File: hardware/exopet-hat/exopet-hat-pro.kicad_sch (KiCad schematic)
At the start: 88 parts, among them J1 12V DC in, J10 CH3 12V OUT, J11 CH4 dry contact, J13 FLOAT1 switch, J14 FLOAT2 switch, J15 pH probe BNC, J3 RPi GPIO (HAT), J4 TEMP (3V3/DATA/GND), J8 CH1 12V OUT, J9 CH2 12V OUT, K1 G5LE-1-CF DC12, K2 G5LE-1-CF DC12, K3 G5LE-1-CF DC12, K4 G5LE-1-CF DC12, Q1 AOD403, U10 MCP6002 (pH buffers), U2 TBD62003AFG, U4 CAT24C32, U5 5V ESD clamp (SOD-323), U6 TPS54302DDC, U7 ADS1115 (floats, 0x48), U8 ADS1115 (pH, 0x49), U9 ISO1540 I2C isolator

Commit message: HAT pro: resolve isolated-rail overvoltage — AMS1117-3.3 LDO on the pH island
Fixes the inline-review finding: the <2mA (<1% load) island let an
unregulated 1W module float past the ADS1115/ISO1540 5.5V max and
inject ripple into the pH ADC. Added U11 AMS1117-3.3 (raw +5V_ISO ->
clean +3V3_ISO); moved U8/U9-VCC2/U10, R26/R27 pull-ups and the R24
bias-top onto +3V3_ISO; C22 = LDO input bulk, C28 = output cap. pH
bias now 1.65V ±0.414V, within ADS1115 FSR and MCP6002 common-mode.
AMS1117's ~15V Vin absorbs the module's no-load rise; ~5mA Iq
preloads it. Netlist confirms the rail split (+5V_ISO = 3 pins only).
ERC benign-only; polarity + golden tables updated. Pin numbers taken
from the KiCad symbol, not assumed (GND1/VO2/VI3). Board layout next.

Co-Authored-By: Claude Fable 5 <noreply@anthropic.com>
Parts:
- added C28: 22uF 10V (LDO out), Capacitor_SMD:C_1210_3225Metric, symbol Device:C
- added U11: AMS1117-3.3 (iso rail), Package_TO_SOT_SMD:SOT-223-3_TabPin2, symbol Regulator_Linear:AMS1117-3.3
- C22: value 10uF 10V -> 10uF 25V (LDO in bulk)
- PS1: value B0505S-1WR2 iso DC-DC (SIP-4) -> 1W iso DC-DC 5Vout SIP-4 (reg or unreg OK; LDO follows)
- R24: value 100k (bias hi) -> 100k (bias hi -> 1.65V mid)
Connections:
- net +5V_ISO: now also U11.3 (VI); no longer C21.1, C25.1, R24.1, R26.1, R27.1, U10.8 (V+), U8.1 (ADDR), U8.8 (VDD), U9.8 (VCC2)
- net ISO_GND: now also C28.2, U11.1 (GND)
- new net +3V3_ISO: C21.1, C25.1, C28.1, R24.1, R26.1, R27.1, U10.8 (V+), U11.2 (VO), U8.1 (ADDR), U8.8 (VDD), U9.8 (VCC2)

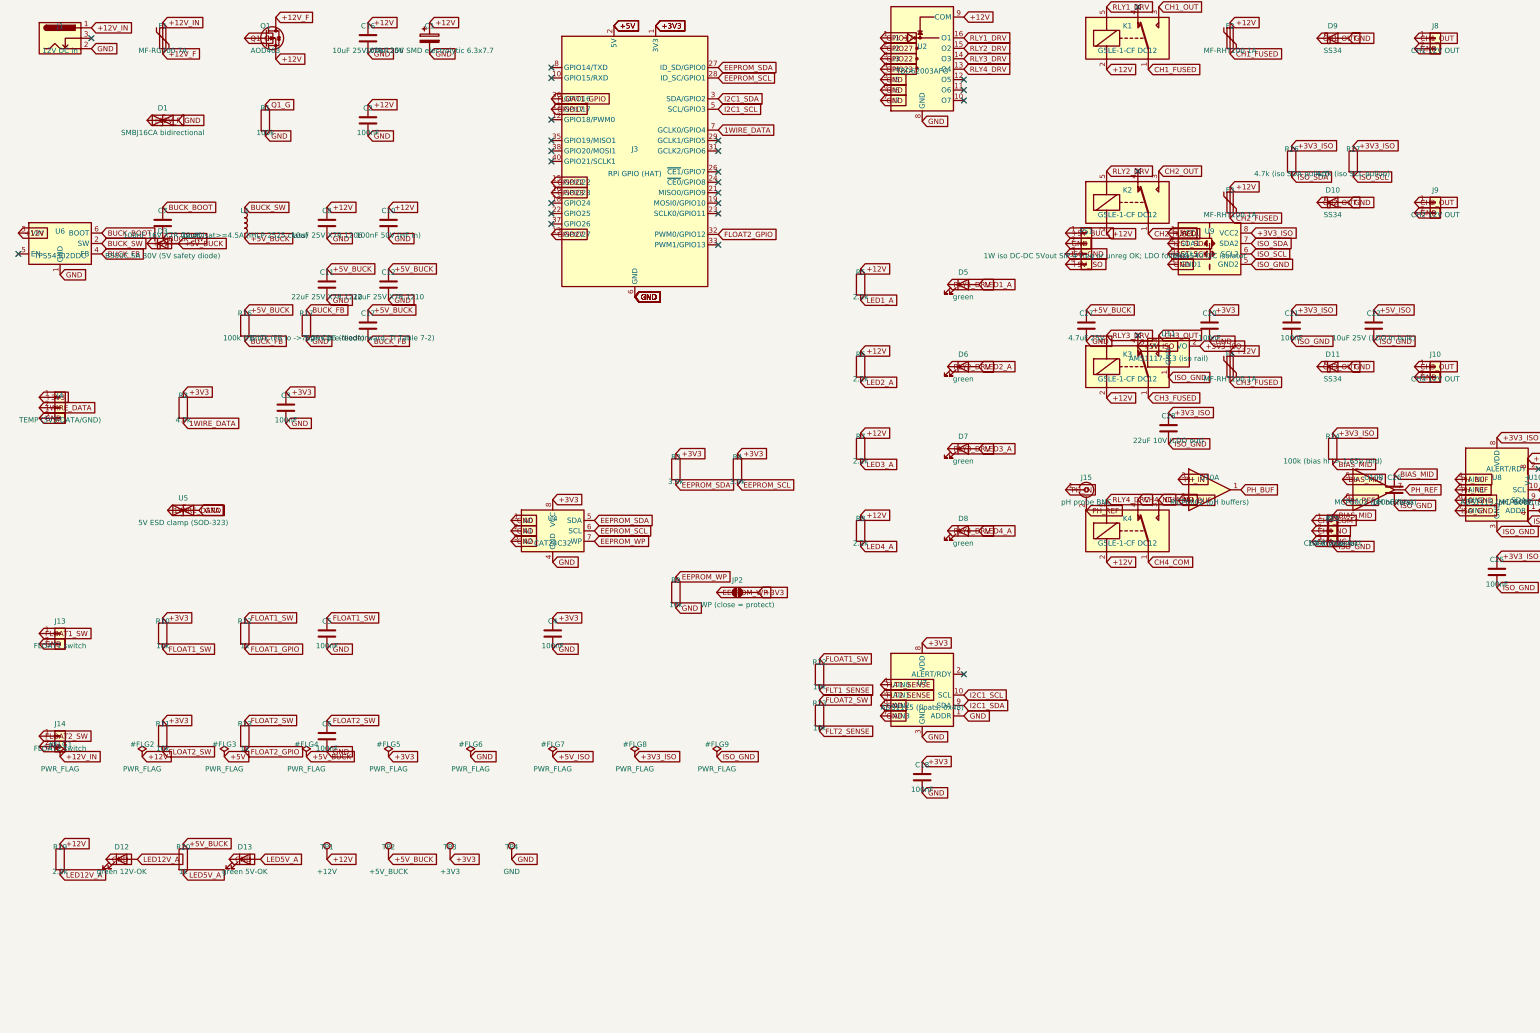
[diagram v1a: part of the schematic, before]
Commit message: HAT pro: expand to 6 relays + 2 more supervised sensor inputs (schematic)
Pro gains CH5 (switched 12V, GPIO24) + CH6 (dry contact, GPIO25) on the
existing TBD62003 driver (now 6/7 channels), each with the standard
fuse/flyback/terminal/LED per their type; and SW3/SW4 general
supervised switch inputs on the sensor ADC's spare A2/A3 channels
(ADC-only, 3-state EOL detection like the floats). J3 pins 18/22 carry
the new GPIO. All 6-relay/sensor parts are add_pro-gated so std stays a
4-relay 65x56 HAT-compliant board. add_pro hoisted above first use
(was NameError-crashing pro generation silently under suppressed
stderr). Both variants: ERC benign-only, golden + polarity clean
(pro-only refs conditionally gated). pro=117 parts, std=79. Board
layout (65x88, 2x3 relays) next.

Co-Authored-By: Claude Fable 5 <noreply@anthropic.com>
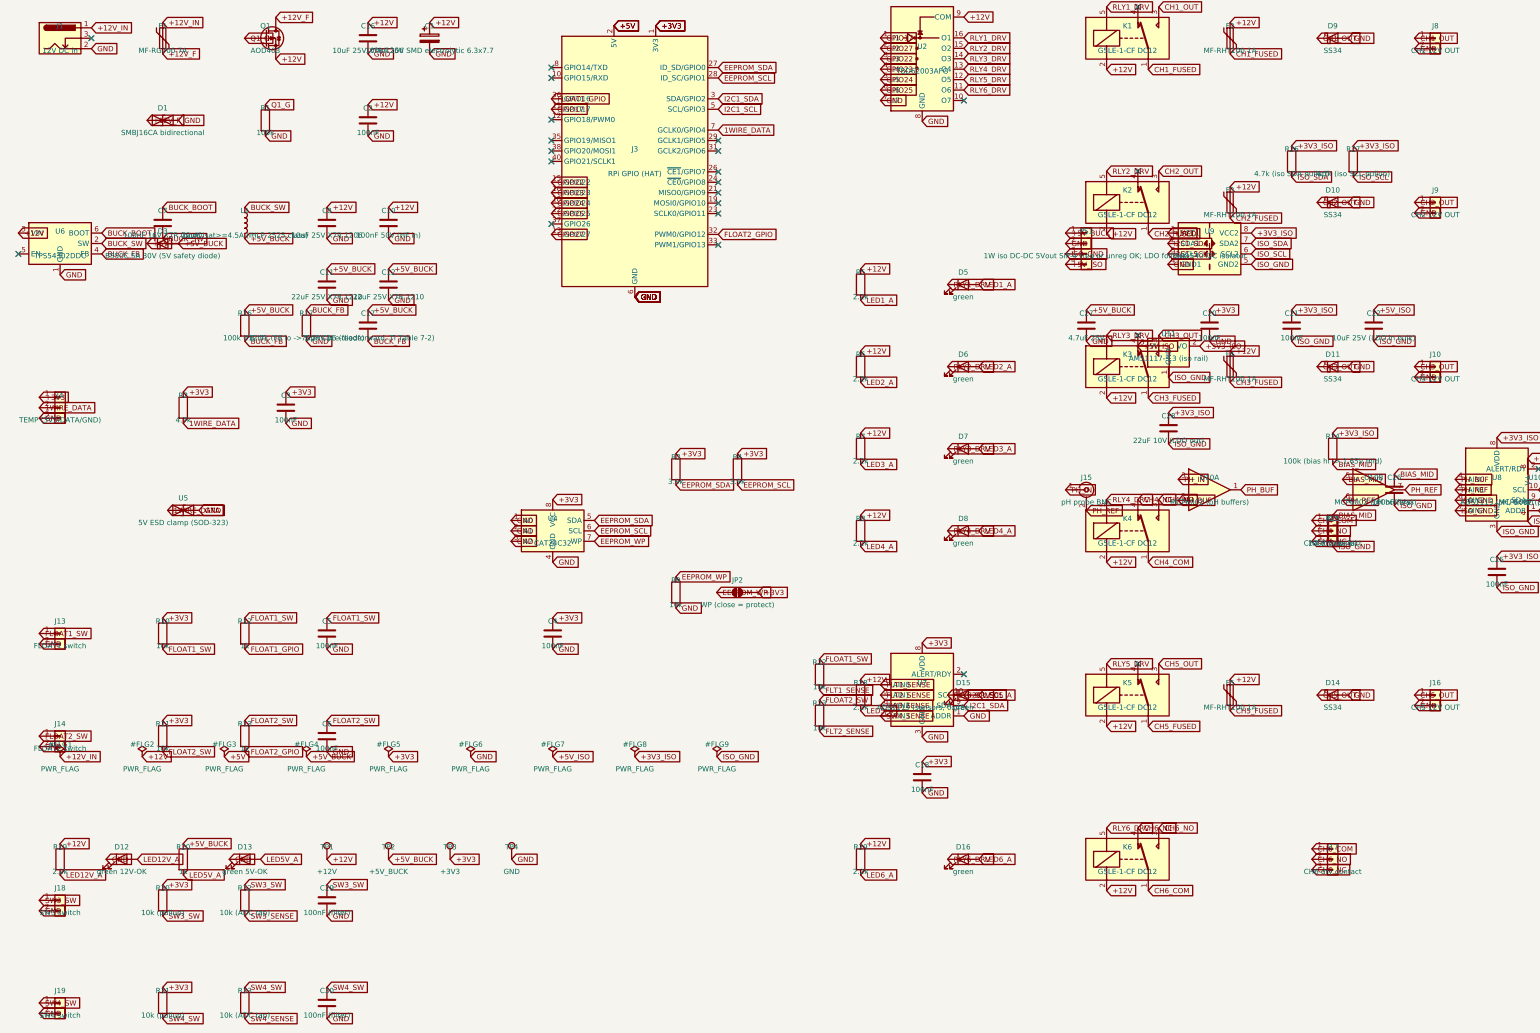
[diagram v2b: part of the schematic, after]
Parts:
- added C29, C30: 100nF (filter), Capacitor_SMD:C_0805_2012Metric, symbol Device:C
- added D14: SS34, Diode_SMD:D_SMA, symbol Device:D_Schottky
- added D15, D16: green, LED_SMD:LED_0805_2012Metric, symbol Device:LED
- added F5: MF-RHT100 1A, Fuse:Fuse_Bourns_MF-RHT100, symbol Device:Polyfuse
- added J16: CH5 12V OUT, TerminalBlock_Phoenix:TerminalBlock_Phoenix_PT-1,5-2-3.5-H_1x02_P3.50mm_Horizontal, symbol Connector_Generic:Conn_01x02
- added J17: CH6 dry contact, TerminalBlock_Phoenix:TerminalBlock_Phoenix_PT-1,5-3-3.5-H_1x03_P3.50mm_Horizontal, symbol Connector_Generic:Conn_01x03
- added J18: SW3 switch, TerminalBlock_Phoenix:TerminalBlock_Phoenix_PT-1,5-2-3.5-H_1x02_P3.50mm_Horizontal, symbol Connector_Generic:Conn_01x02
- added J19: SW4 switch, TerminalBlock_Phoenix:TerminalBlock_Phoenix_PT-1,5-2-3.5-H_1x02_P3.50mm_Horizontal, symbol Connector_Generic:Conn_01x02
- added K5, K6: G5LE-1-CF DC12, Relay_THT:Relay_SPDT_Omron-G5LE-1, symbol Relay:G5LE-1
- added R28, R29: 2.2k, Resistor_SMD:R_0805_2012Metric, symbol Device:R
- added R30, R31: 10k (pullup), Resistor_SMD:R_0805_2012Metric, symbol Device:R
- added R32, R33: 10k (ADC tap), Resistor_SMD:R_0805_2012Metric, symbol Device:R
- U7: value ADS1115 (floats, 0x48) -> ADS1115 (sensors, 0x48)
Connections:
- net +12V: now also F5.1, K5.2, K6.2, R28.1, R29.1
- net +3V3: now also R30.1, R31.1
- net GND: now also C29.2, C30.2, D14.2 (A), J16.2 (Pin_2), J18.2 (Pin_2), J19.2 (Pin_2); no longer U2.5 (I5), U2.6 (I6), U7.6 (AIN2), U7.7 (AIN3)
- net GPIO24: now reaches J3.18 (GPIO24)
- net GPIO24: now also U2.5 (I5)
- net GPIO25: now reaches J3.22 (GPIO25)
- net GPIO25: now also U2.6 (I6)
- net RLY6_DRV: now reaches U2.11 (O6)
- net RLY6_DRV: now also D16.1 (K), K6.5
- net RLY5_DRV: now reaches U2.12 (O5)
- net RLY5_DRV: now also D15.1 (K), K5.5
- new net CH5_FUSED: F5.2, K5.1
- new net CH5_OUT: D14.1 (K), J16.1 (Pin_1), K5.3
- new net CH6_COM: J17.1 (Pin_1), K6.1
- new net CH6_NC: J17.3 (Pin_3), K6.4
- new net CH6_NO: J17.2 (Pin_2), K6.3
- new net LED5_A: D15.2 (A), R28.2
- new net LED6_A: D16.2 (A), R29.2
- new net SW3_SENSE: R32.2, U7.6 (AIN2)
- new net SW3_SW: C29.1, J18.1 (Pin_1), R30.2, R32.1
- new net SW4_SENSE: R33.2, U7.7 (AIN3)
- new net SW4_SW: C30.1, J19.1 (Pin_1), R31.2, R33.1
- no-connect marks 27 -> 24

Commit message: HAT pro layout WIP: 65x92 floorplan established (NOT placement-clean)
Custom tight BNC edge-launch footprint (KiCad's have 37mm phantom
bboxes). Board grows to 65x92: the Pi's fixed y52.5 mounting hole
forced relay row 3 (K5/K6) down to y64.5, which opens the y42-56
mid-gap for the channel fuses. 6 relay terminals in two front rows +
BNC front-right; SW3/SW4 sensor terminals on row 2; pH island back-side
under the front region. Edge connectors (terminals + BNC) added to the
offboard allow-list since their wire-entry/barrel is meant to overhang.
Generates + flips (108 parts); ~45 placement collisions remain to
iterate. Deliberately WIP — not gated, routed, or fab'd.

Co-Authored-By: Claude Fable 5 <noreply@anthropic.com>
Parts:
- J15: footprint Connector_Coaxial:BNC_Amphenol_031-6575_Horizontal -> ExoPet:BNC_Edge_ExoPet
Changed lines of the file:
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@@
     (property "Reference" "J15" (at 280 147 0) (effects (font (size 1.27 1.27))))
     (property "Value" "pH probe BNC" (at 280 153 0) (effects (font (size 1.27 1.27))))
-    (property "Footprint" "Connector_Coaxial:BNC_Amphenol_031-6575_Horizontal" (at 280 150 0) (effects (font (size 1.27 1.27)) hide))
+    (property "Footprint" "ExoPet:BNC_Edge_ExoPet" (at 280 150 0) (effects (font (size 1.27 1.27)) hide))
     (property "LCSC" "VERIFY" (at 280 150 0) (effects (font (size 1.27 1.27)) hide))
     (pin "1")
